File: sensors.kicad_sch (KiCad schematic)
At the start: 21 parts, among them U2 LIS2DH12TR, U3 L3GD20HTR, U4 MP6515GF-Z, U5 MP6515GF-Z, U6 MP6515GF-Z

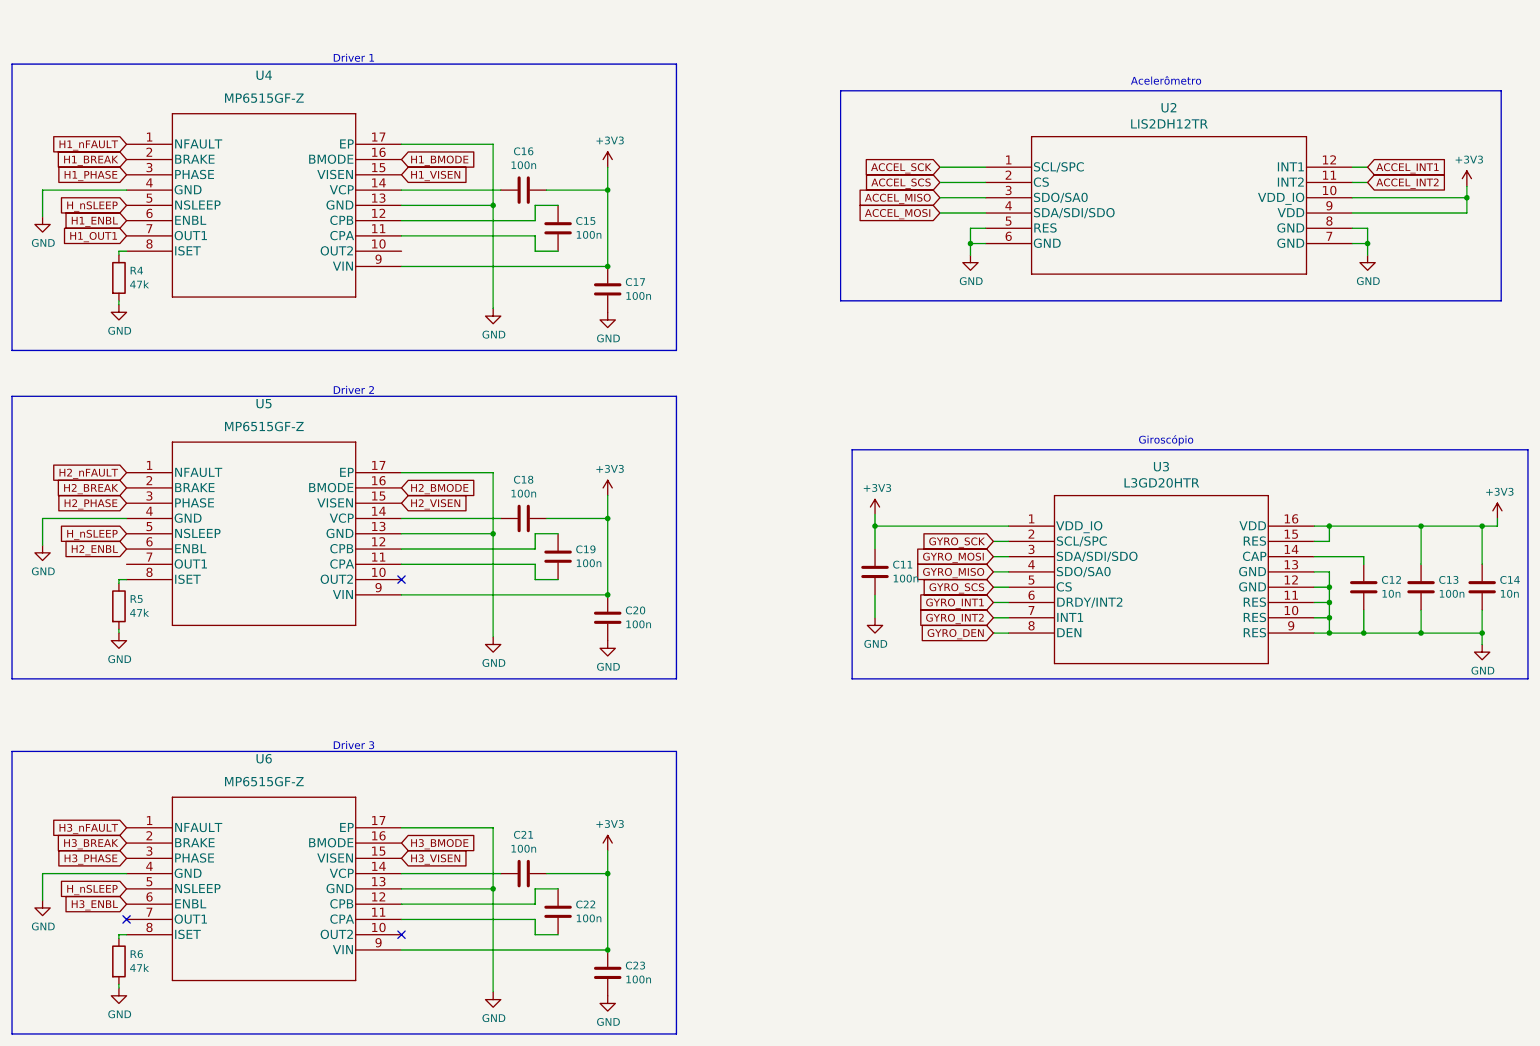
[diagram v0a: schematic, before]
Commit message: schematic update hall sensor
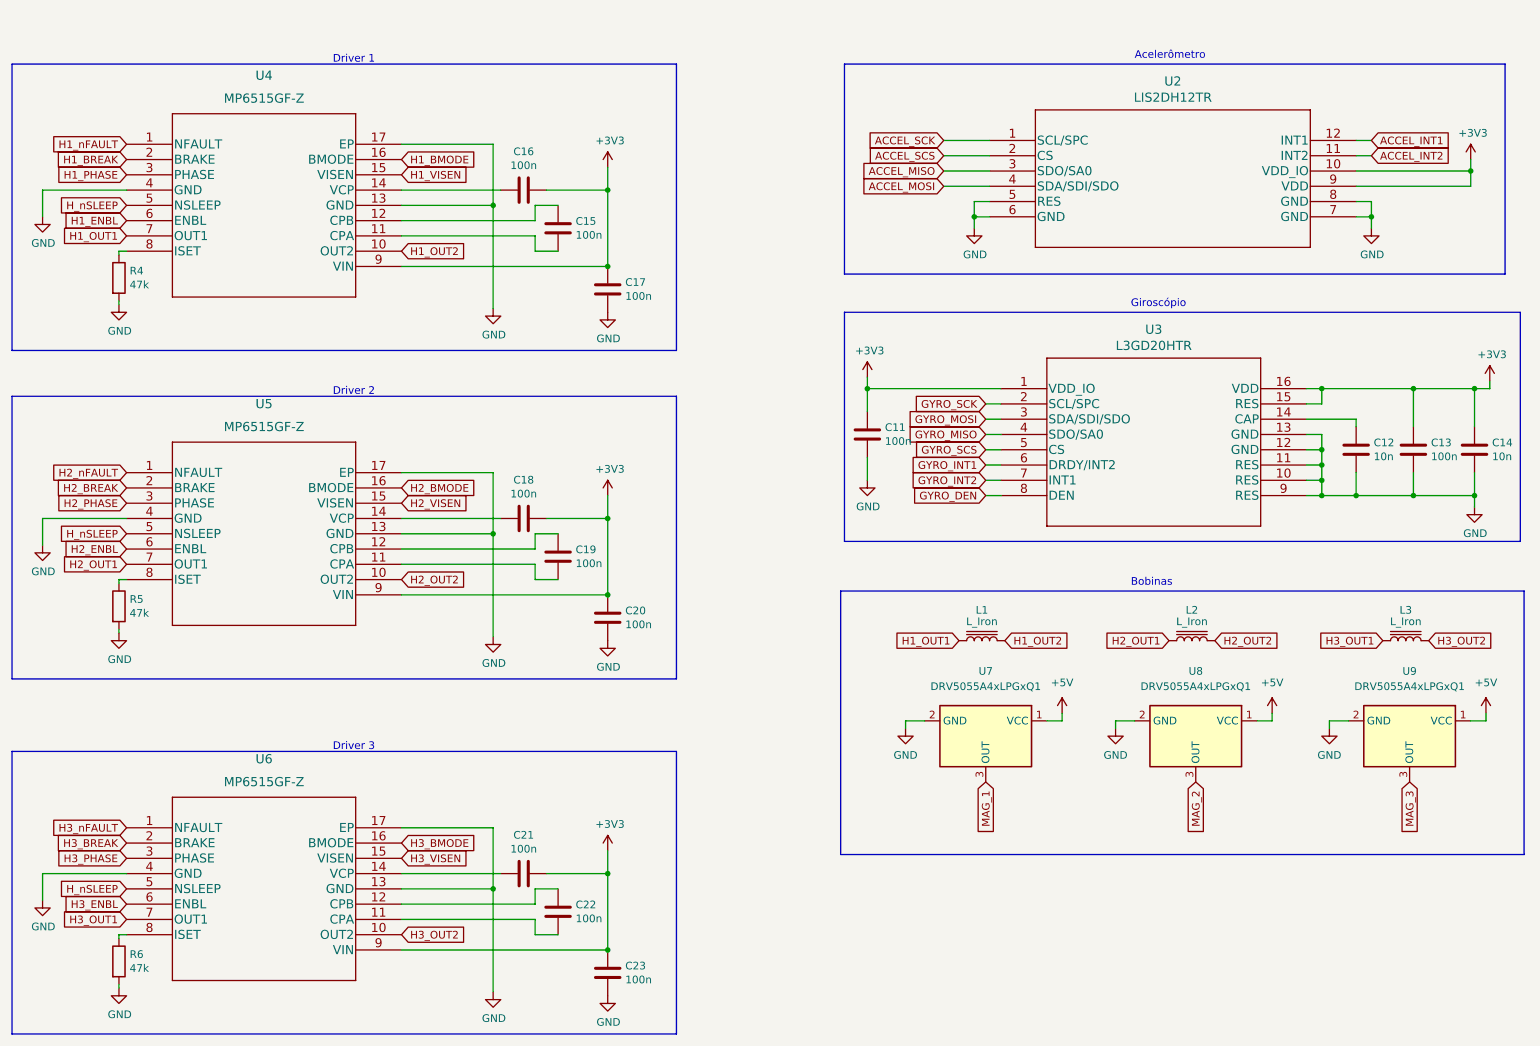
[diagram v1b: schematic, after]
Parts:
- added L1, L2, L3: L_Iron, symbol Device:L_Iron
- added U7, U8, U9: DRV5055A4xLPGxQ1, Package_TO_SOT_THT:TO-92_Inline, symbol Sensor_Magnetic:DRV5055A4xLPGxQ1
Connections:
- net GND: now also U7.2 (GND), U8.2 (GND), U9.2 (GND)
- net H1_OUT1: now also L1.1
- net H1_OUT2: now reaches U4.10 (OUT2)
- net H1_OUT2: now also L1.2
- net H2_OUT2: now reaches U5.10 (OUT2)
- net H2_OUT2: now also L2.2
- net H2_OUT1: now reaches U5.7 (OUT1)
- net H2_OUT1: now also L2.1
- net H3_OUT2: now reaches U6.10 (OUT2)
- net H3_OUT2: now also L3.2
- net H3_OUT1: now reaches U6.7 (OUT1)
- net H3_OUT1: now also L3.1
- new net +5V: U7.1 (VCC), U8.1 (VCC), U9.1 (VCC)
- new net MAG_1: U7.3 (OUT)
- new net MAG_2: U8.3 (OUT)
- new net MAG_3: U9.3 (OUT)
- no-connect marks 3 -> 0
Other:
- note added: "Bobinas"
- moved on the sheet: C11, C12, C13, C14, U2, U3

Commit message: start layout
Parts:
- L1, L2, L3: footprint (none) -> magnetorque_lib:magnetorquer
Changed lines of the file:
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@@
     (property "Reference" "L2" (id 0) (at 215.265 119.38 90))
     (property "Value" "L_Iron" (id 1) (at 215.265 121.285 90))
-    (property "Footprint" "" (id 2) (at 215.265 124.46 0)
+    (property "Footprint" "magnetorque_lib:magnetorquer" (id 2) (at 215.265 124.46 0)
       (effects (font (size 1.27 1.27)) hide)
     )
@@
     (property "Reference" "L3" (id 0) (at 250.825 119.38 90))
     (property "Value" "L_Iron" (id 1) (at 250.825 121.285 90))
-    (property "Footprint" "" (id 2) (at 250.825 124.46 0)
+    (property "Footprint" "magnetorque_lib:magnetorquer" (id 2) (at 250.825 124.46 0)
       (effects (font (size 1.27 1.27)) hide)
     )
@@
     (property "Reference" "L1" (id 0) (at 180.34 119.38 90))
     (property "Value" "L_Iron" (id 1) (at 180.34 121.285 90))
-    (property "Footprint" "" (id 2) (at 180.34 124.46 0)
-      (effects (font (size 1.27 1.27)) hide)
-    )
+    (property "Footprint" "magnetorque_lib:magnetorquer" (id 2) (at 180.34 124.46 0)
+      (effects (font (size 1.27 1.27)) hide)
+    )

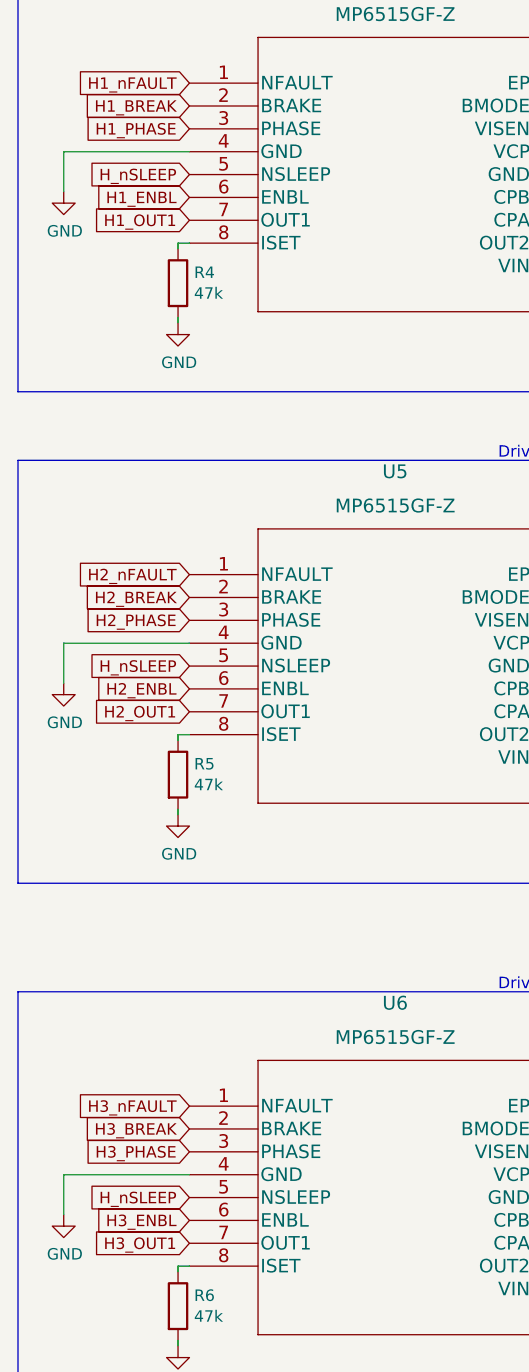
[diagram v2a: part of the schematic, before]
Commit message: adicionado conector pc104
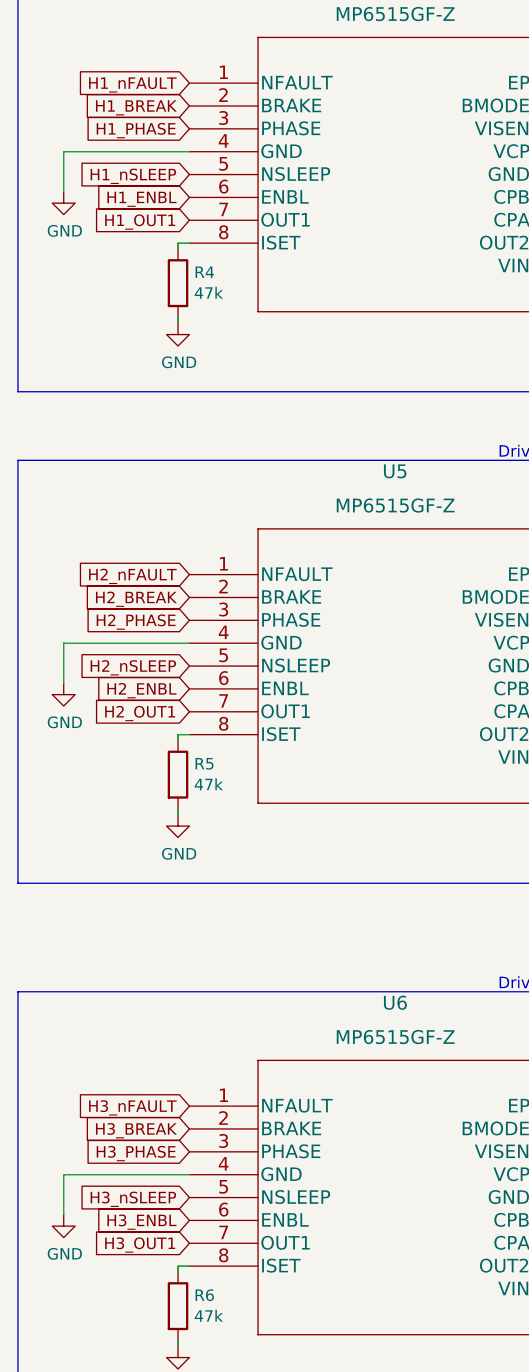
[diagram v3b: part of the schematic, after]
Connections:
- removed net H_nSLEEP: U4.5 (NSLEEP), U5.5 (NSLEEP), U6.5 (NSLEEP)
- new net H1_nSLEEP: U4.5 (NSLEEP)
- new net H2_nSLEEP: U5.5 (NSLEEP)
- new net H3_nSLEEP: U6.5 (NSLEEP)
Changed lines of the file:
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@@
     )
   )
-  (global_label "H_nSLEEP" (shape input) (at 38.1 106.68 180) (fields_autoplaced)
+  (global_label "H2_nSLEEP" (shape input) (at 38.1 106.68 180) (fields_autoplaced)
     (effects (font (size 1.27 1.27)) (justify right))
-    (property "Intersheet References" "${INTERSHEET_REFS}" (id 0) (at 26.5229 106.6006 0)
+    (property "Intersheet References" "${INTERSHEET_REFS}" (id 0) (at 25.3134 106.6006 0)
       (effects (font (size 1.27 1.27)) (justify right) hide)
     )
@@
     )
   )
-  (global_label "H_nSLEEP" (shape input) (at 38.1 52.07 180) (fields_autoplaced)
+  (global_label "H1_nSLEEP" (shape input) (at 38.1 52.07 180) (fields_autoplaced)
     (effects (font (size 1.27 1.27)) (justify right))
-    (property "Intersheet References" "${INTERSHEET_REFS}" (id 0) (at 0 0 0)
-      (effects (font (size 1.27 1.27)) hide)
+    (property "Intersheet References" "${INTERSHEET_REFS}" (id 0) (at 25.3134 51.9906 0)
+      (effects (font (size 1.27 1.27)) (justify right) hide)
     )
   )
@@
     )
   )
-  (global_label "H_nSLEEP" (shape input) (at 38.1 165.735 180) (fields_autoplaced)
+  (global_label "H3_nSLEEP" (shape input) (at 38.1 165.735 180) (fields_autoplaced)
     (effects (font (size 1.27 1.27)) (justify right))
-    (property "Intersheet References" "${INTERSHEET_REFS}" (id 0) (at 26.5229 165.6556 0)
+    (property "Intersheet References" "${INTERSHEET_REFS}" (id 0) (at 25.3134 165.6556 0)
       (effects (font (size 1.27 1.27)) (justify right) hide)
     )

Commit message: last commit
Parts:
- removed C15, C16, C17, C18, C19, C20, C21, C22, C23: 100n, Capacitor_SMD:C_0805_2012Metric, symbol Device:C
- removed L1, L2, L3: L_Iron, magnetorque_lib:magnetorquer, symbol Device:L_Iron
- removed R4, R5, R6: 47k, Resistor_SMD:R_0805_2012Metric, symbol Device:R
- removed U4, U5, U6: MP6515GF-Z, magnetorque_lib:MP6515GF-Z, symbol mp65:MP6515GF-Z
- removed U9: DRV5055A4xLPGxQ1, Package_TO_SOT_THT:TO-92_Inline, symbol Sensor_Magnetic:DRV5055A4xLPGxQ1
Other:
- note added: "Magnetômetro-HAL"
- note removed: "Bobinas"
- note removed: "Driver 1"
- note removed: "Driver 2"
- note removed: "Driver 3"
- moved on the sheet: C11, C12, C13, C14, U2, U3, U7, U8
